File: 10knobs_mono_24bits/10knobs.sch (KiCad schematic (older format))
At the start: 42 parts, among them J1 Conn_01x06_Female, U1 MCP4822, U2 BluePill_STM32F103C, U3 6N138, U4 LM358

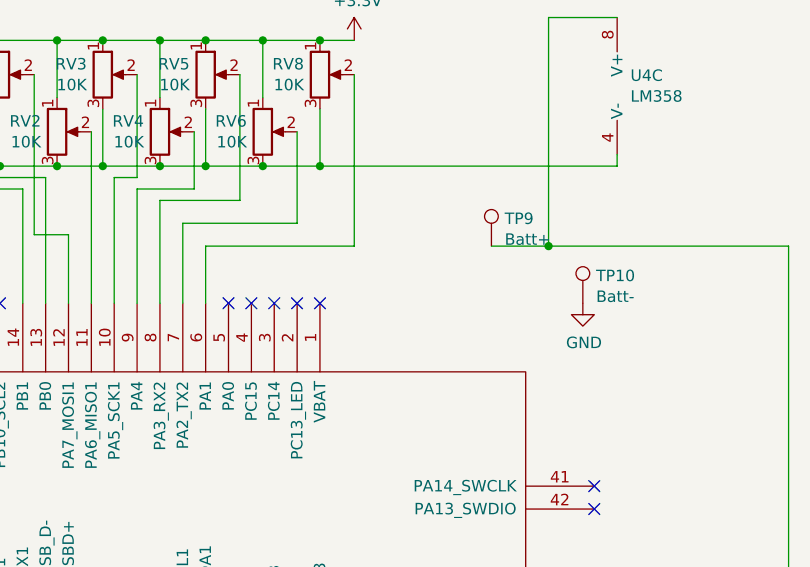
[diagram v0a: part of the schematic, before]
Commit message: Added PCB, final corrections
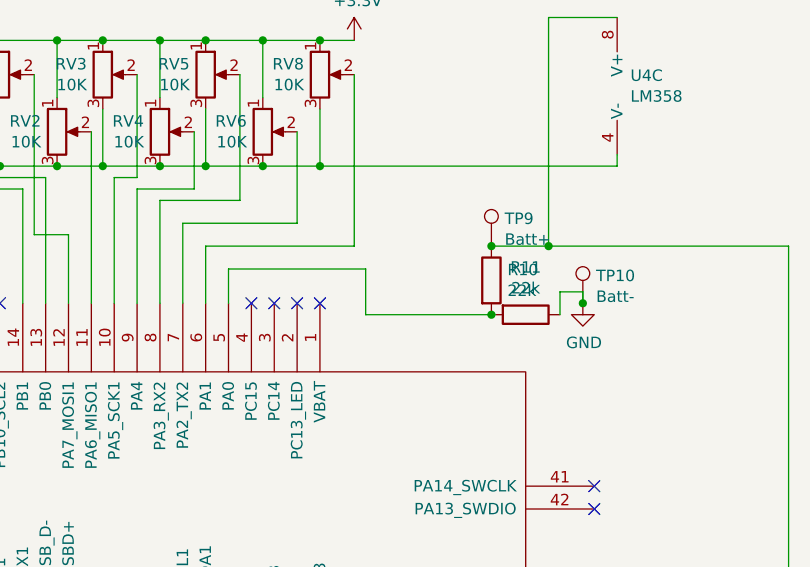
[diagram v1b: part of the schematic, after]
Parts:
- added R10, R11: 22k, Resistor_THT:R_Axial_DIN0207_L6.3mm_D2.5mm_P7.62mm_Horizontal, symbol Device:R
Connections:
- net GND: now also R11.1
- net at C1.1, C2.1, TP9.1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: now also R10.1
- net at U2.5 (PA0): now also R10.2, R11.2
- no-connect marks 23 -> 22
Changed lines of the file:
@@
 Wire Wire Line
 	8500 2000 8750 2000
-NoConn ~ 8350 3150
 Wire Wire Line
 	7350 2000 7600 2000
@@
 Wire Wire Line
 	6750 3100 6850 3100
+$Comp
+L Device:R R10
+U 1 1 5F41B0F0
+P 9500 3050
+F 0 "R10" H 9570 3096 50  0000 L CNN
+F 1 "22k" H 9570 3005 50  0000 L CNN
+F 2 "Resistor_THT:R_Axial_DIN0207_L6.3mm_D2.5mm_P7.62mm_Horizontal" V 9430 3050 50  0001 C CNN
+F 3 "~" H 9500 3050 50  0001 C CNN
+	1    9500 3050
+	1    0    0    -1
+$EndComp
+Connection ~ 9500 2900
+$Comp
+L Device:R R11
+U 1 1 5F41B1C3
+P 9650 3200
+F 0 "R11" V 9443 3200 50  0000 C CNN
+F 1 "22k" V 9534 3200 50  0000 C CNN
+F 2 "Resistor_THT:R_Axial_DIN0207_L6.3mm_D2.5mm_P7.62mm_Horizontal" V 9580 3200 50  0001 C CNN
+F 3 "~" H 9650 3200 50  0001 C CNN
+	1    9650 3200
+	0    1    1    0
+$EndComp
+Wire Wire Line
+	9900 3100 9800 3100
+Wire Wire Line
+	9800 3100 9800 3200
+Wire Wire Line
+	9900 3150 9900 3100
+Connection ~ 9900 3150
+Wire Wire Line
+	9500 3200 8950 3200
+Wire Wire Line
+	8950 3200 8950 3000
+Wire Wire Line
+	8950 3000 8350 3000
+Wire Wire Line
+	8350 3000 8350 3150
+Connection ~ 9500 3200
 $EndSCHEMATC
